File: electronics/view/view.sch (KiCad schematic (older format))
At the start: 90 parts, among them J1 BLDC, J2 USB_C_Receptacle_USB2.0, J3 LCD, J4 Strain, J5 Strain, Q1 MMBT4403, Q2 UMH3N, U1 MT6701-CT, U2 T-Micro32_Plus, U3 CH340C, U4 HX711, U5 TMC6300, U6 AP1117-33, U7 SN74LV1T34DBV, U8 VEML7700

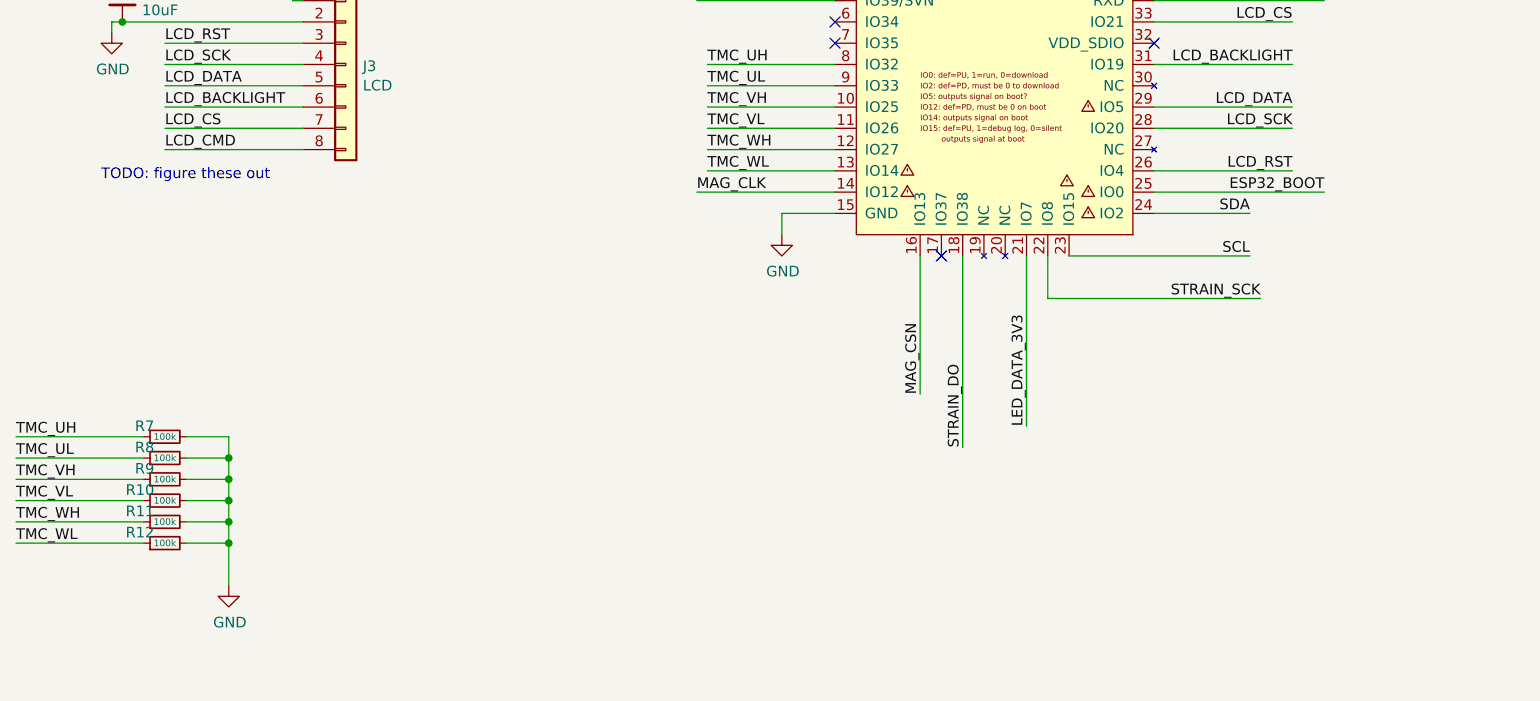
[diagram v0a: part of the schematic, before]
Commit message: View: Update pin assignments on ESP32 to avoid potential boot issues
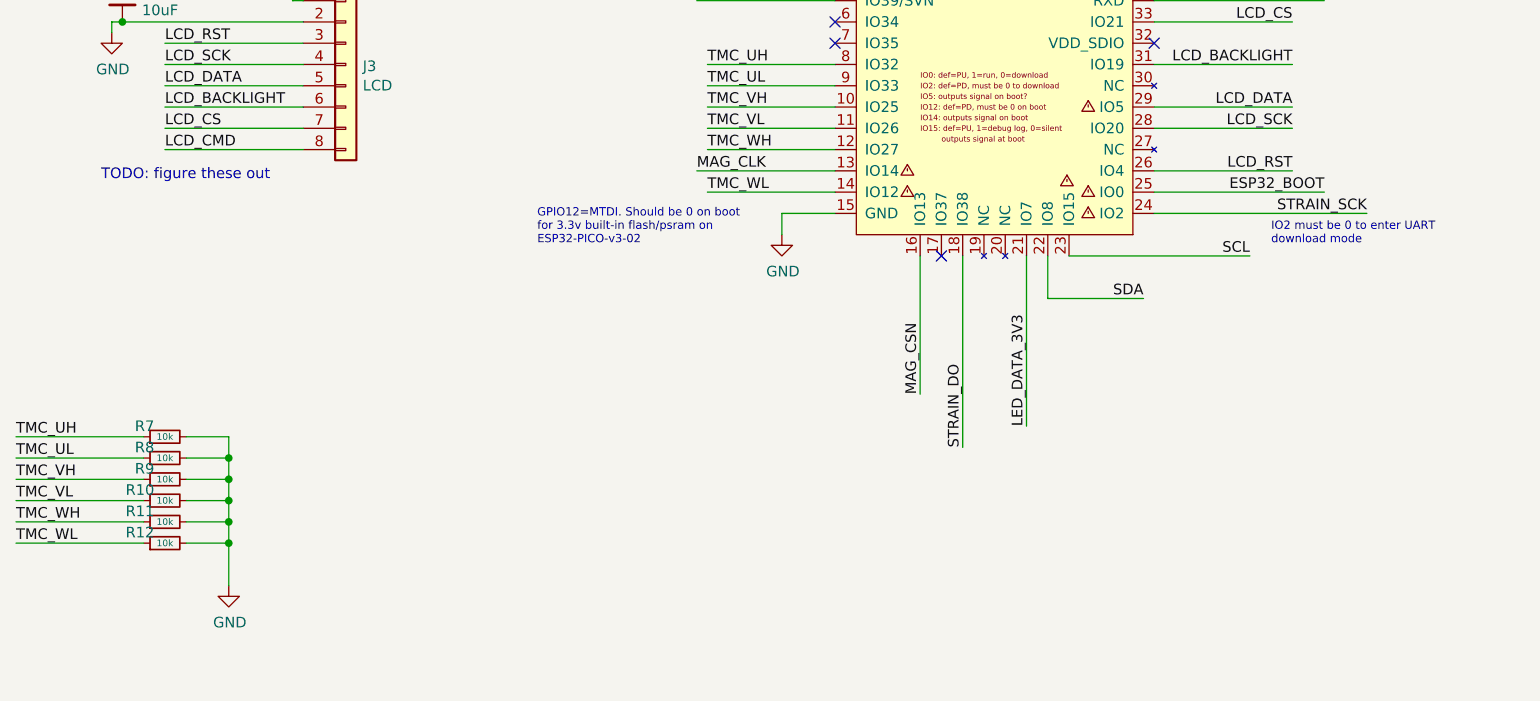
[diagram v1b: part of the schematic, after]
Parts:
- R10, R11, R12, R7, R8, R9: value 100k -> 10k
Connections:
- net MAG_CLK: now also U2.13 (IO14); no longer U2.14 (IO12)
- net SDA: now also U2.22 (IO8); no longer U2.24 (IO2)
- net STRAIN_SCK: now also U2.24 (IO2); no longer U2.22 (IO8)
- net TMC_WL: now also U2.14 (IO12); no longer U2.13 (IO14)
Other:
- note added: "GPIO12=MTDI. Should be 0 on boot\nfor 3.3v built-in flash/psram on\nESP32-PICO-v3-02"
- note added: "IO2 must be 0 to enter UART\ndownload mode"
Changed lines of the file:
@@
 TMC_WH
 Wire Wire Line
-	13050 3450 12450 3450
-Text Label 12450 3450 0    50   ~ 0
+	13050 3550 12450 3550
+Text Label 12450 3550 0    50   ~ 0
 TMC_WL
 Wire Wire Line
@@
 	13450 3850 13450 4500
 Wire Wire Line
-	13050 3550 12400 3550
+	13050 3450 12400 3450
 Wire Wire Line
 	13050 2650 12400 2650
 Text Label 13450 4500 1    50   ~ 0
 MAG_CSN
-Text Label 12400 3550 0    50   ~ 0
+Text Label 12400 3450 0    50   ~ 0
 MAG_CLK
 Text Label 12400 2650 0    50   ~ 0
@@
 Text Label 13650 4750 1    50   ~ 0
 STRAIN_DO
-Text Label 15050 4050 2    50   ~ 0
+Text Label 15550 3650 2    50   ~ 0
 STRAIN_SCK
 Wire Wire Line
-	14050 4050 15050 4050
+	14550 3650 15550 3650
 Wire Wire Line
 	13950 4650 13950 3850
@@
 P 9900 4700
 F 0 "R7" V 9950 4750 50  0000 L CNN
-F 1 "100k" V 9900 4700 31  0000 C CNN
+F 1 "10k" V 9900 4700 31  0000 C CNN
 F 2 "Resistor_SMD:R_0603_1608Metric" H 9900 4700 50  0001 C CNN
 F 3 "~" H 9900 4700 50  0001 C CNN
@@
 P 9900 4800
 F 0 "R8" V 9950 4850 50  0000 L CNN
-F 1 "100k" V 9900 4800 31  0000 C CNN
+F 1 "10k" V 9900 4800 31  0000 C CNN
 F 2 "Resistor_SMD:R_0603_1608Metric" H 9900 4800 50  0001 C CNN
 F 3 "~" H 9900 4800 50  0001 C CNN
@@
 P 9900 4900
 F 0 "R9" V 9950 4950 50  0000 L CNN
-F 1 "100k" V 9900 4900 31  0000 C CNN
+F 1 "10k" V 9900 4900 31  0000 C CNN
 F 2 "Resistor_SMD:R_0603_1608Metric" H 9900 4900 50  0001 C CNN
 F 3 "~" H 9900 4900 50  0001 C CNN
@@
 P 9900 5000
 F 0 "R10" V 9950 5050 50  0000 L CNN
-F 1 "100k" V 9900 5000 31  0000 C CNN
+F 1 "10k" V 9900 5000 31  0000 C CNN
 F 2 "Resistor_SMD:R_0603_1608Metric" H 9900 5000 50  0001 C CNN
 F 3 "~" H 9900 5000 50  0001 C CNN
@@
 P 9900 5100
 F 0 "R11" V 9950 5150 50  0000 L CNN
-F 1 "100k" V 9900 5100 31  0000 C CNN
+F 1 "10k" V 9900 5100 31  0000 C CNN
 F 2 "Resistor_SMD:R_0603_1608Metric" H 9900 5100 50  0001 C CNN
 F 3 "~" H 9900 5100 50  0001 C CNN
@@
 P 9900 5200
 F 0 "R12" V 9950 5250 50  0000 L CNN
-F 1 "100k" V 9900 5200 31  0000 C CNN
+F 1 "10k" V 9900 5200 31  0000 C CNN
 F 2 "Resistor_SMD:R_0603_1608Metric" H 9900 5200 50  0001 C CNN
 F 3 "~" H 9900 5200 50  0001 C CNN
@@
 	14050 4050 14050 3850
 Wire Wire Line
-	14550 3650 15000 3650
+	14050 4050 14500 4050
 Wire Wire Line
 	14150 3850 15000 3850
-Text Label 15000 3650 2    50   ~ 0
+Text Label 14500 4050 2    50   ~ 0
 SDA
 Text Label 15000 3850 2    50   ~ 0
@@
 Wire Wire Line
 	2650 1050 2650 1150
+Text Notes 11650 3800 0    39   ~ 0
+GPIO12=MTDI. Should be 0 on boot\nfor 3.3v built-in flash/psram on\nESP32-PICO-v3-02
+Text Notes 15100 3800 0    39   ~ 0
+IO2 must be 0 to enter UART\ndownload mode
 $EndSCHEMATC

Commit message: View: PCB checkpoint
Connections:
- net MAG_CLK: now also U2.16 (IO13); no longer U2.13 (IO14)
- net MAG_CSN: now also U2.13 (IO14); no longer U2.16 (IO13)
- net MAG_DO: now also U2.17 (IO37); no longer U2.5 (IO39/SVN)
- net SCL: now also U2.22 (IO8); no longer U2.23 (IO15)
- net SDA: now also U2.23 (IO15); no longer U2.22 (IO8)
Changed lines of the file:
@@
 LCD_CMD
 Wire Wire Line
+	13050 3450 12400 3450
+Wire Wire Line
 	13450 3850 13450 4500
 Wire Wire Line
-	13050 3450 12400 3450
-Wire Wire Line
-	13050 2650 12400 2650
+	13550 3850 13550 4500
+Text Label 12400 3450 0    50   ~ 0
+MAG_CSN
 Text Label 13450 4500 1    50   ~ 0
-MAG_CSN
-Text Label 12400 3450 0    50   ~ 0
 MAG_CLK
-Text Label 12400 2650 0    50   ~ 0
+Text Label 13550 4500 1    50   ~ 0
 MAG_DO
 Text Label 13650 4750 1    50   ~ 0
@@
 	14050 4050 14050 3850
 Wire Wire Line
-	14050 4050 14500 4050
-Wire Wire Line
-	14150 3850 15000 3850
-Text Label 14500 4050 2    50   ~ 0
+	14150 3850 14600 3850
+Wire Wire Line
+	14050 4050 14900 4050
+Text Label 14600 3850 2    50   ~ 0
 SDA
-Text Label 15000 3850 2    50   ~ 0
+Text Label 14900 4050 2    50   ~ 0
 SCL
 NoConn ~ 14550 2850
 NoConn ~ 13050 2750
 NoConn ~ 13050 2850
-NoConn ~ 13550 3850
 $Comp
 L power:PWR_FLAG #FLG0101
@@
 Text Notes 15100 3800 0    39   ~ 0
 IO2 must be 0 to enter UART\ndownload mode
+NoConn ~ 13050 2650
 $EndSCHEMATC

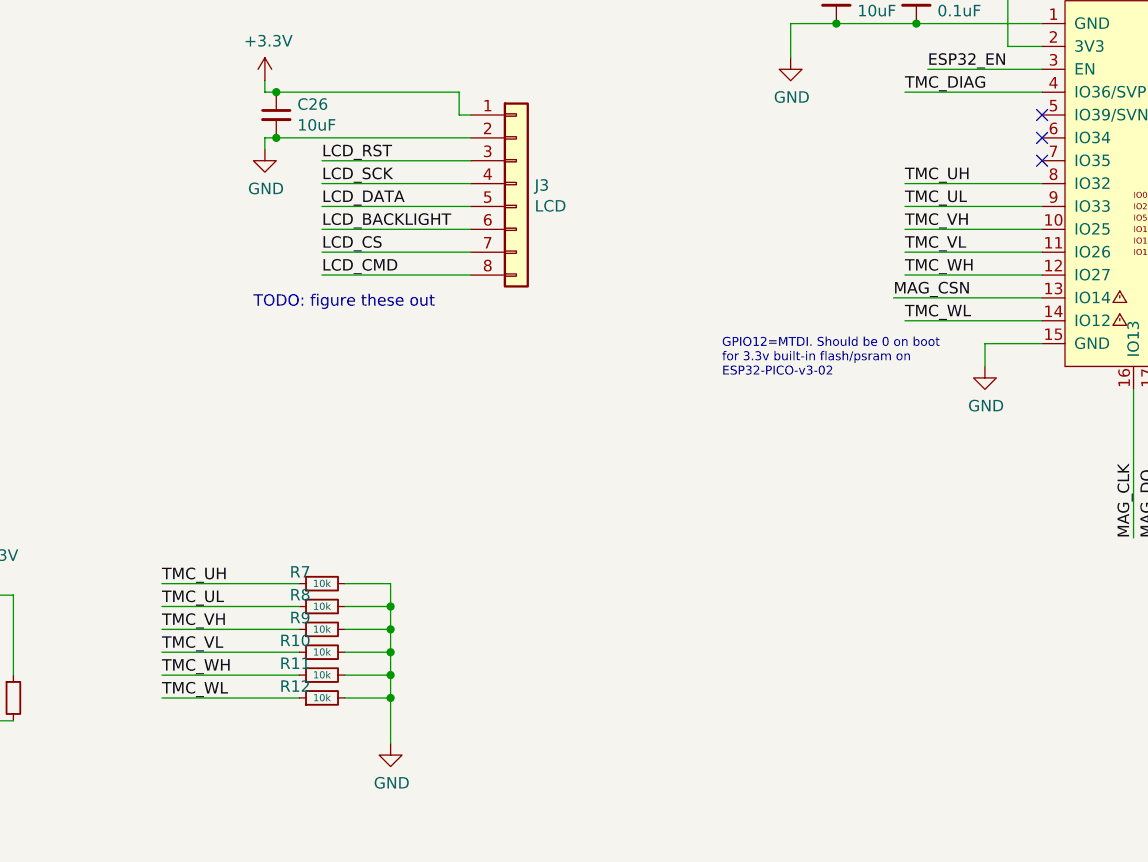
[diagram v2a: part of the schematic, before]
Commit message: View: finished initial routing
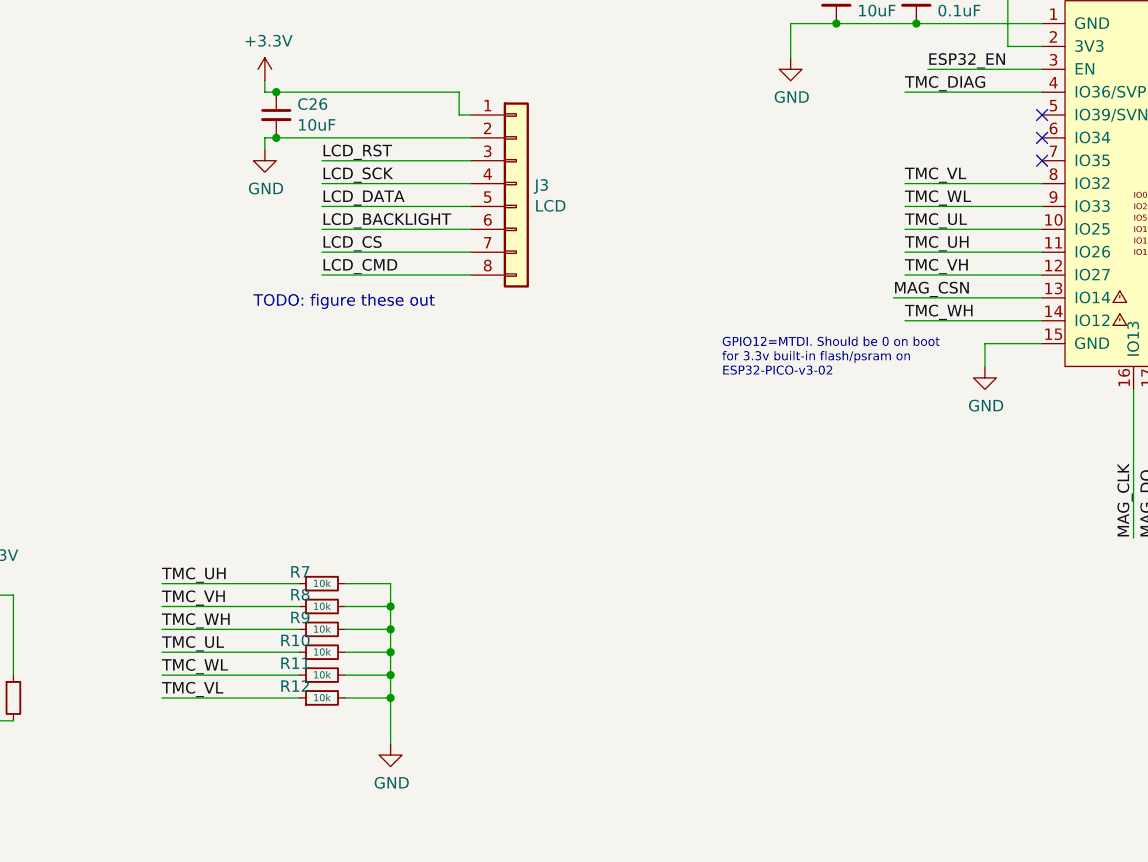
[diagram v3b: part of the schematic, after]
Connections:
- net TMC_UH: now also U2.11 (IO26); no longer U2.8 (IO32)
- net TMC_UL: now also R10.1, U2.10 (IO25); no longer R8.1, U2.9 (IO33)
- net TMC_VH: now also R8.1, U2.12 (IO27); no longer R9.1, U2.10 (IO25)
- net TMC_VL: now also R12.1, U2.8 (IO32); no longer R10.1, U2.11 (IO26)
- net TMC_WH: now also R9.1, U2.14 (IO12); no longer R11.1, U2.12 (IO27)
- net TMC_WL: now also R11.1, U2.9 (IO33); no longer R12.1, U2.14 (IO12)
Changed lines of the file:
@@
 	6700 6500 7050 6500
+Wire Wire Line
+	13050 3150 12450 3150
+Text Label 12450 3150 0    50   ~ 0
+TMC_UL
+Wire Wire Line
+	13050 3350 12450 3350
+Text Label 12450 3350 0    50   ~ 0
+TMC_VH
 Wire Wire Line
 	13050 2950 12450 2950
 Text Label 12450 2950 0    50   ~ 0
-TMC_UH
+TMC_VL
+Wire Wire Line
+	13050 3550 12450 3550
+Text Label 12450 3550 0    50   ~ 0
+TMC_WH
 Wire Wire Line
 	13050 3050 12450 3050
 Text Label 12450 3050 0    50   ~ 0
-TMC_UL
-Wire Wire Line
-	13050 3150 12450 3150
-Text Label 12450 3150 0    50   ~ 0
-TMC_VH
-Wire Wire Line
-	13050 3250 12450 3250
-Text Label 12450 3250 0    50   ~ 0
-TMC_VL
-Wire Wire Line
-	13050 3350 12450 3350
-Text Label 12450 3350 0    50   ~ 0
-TMC_WH
-Wire Wire Line
-	13050 3550 12450 3550
-Text Label 12450 3550 0    50   ~ 0
 TMC_WL
 Wire Wire Line
@@
 TMC_UH
 Wire Wire Line
+	9800 5000 9200 5000
+Text Label 9200 5000 0    50   ~ 0
+TMC_UL
+Wire Wire Line
 	9800 4800 9200 4800
 Text Label 9200 4800 0    50   ~ 0
-TMC_UL
+TMC_VH
+Wire Wire Line
+	9800 5200 9200 5200
+Text Label 9200 5200 0    50   ~ 0
+TMC_VL
 Wire Wire Line
 	9800 4900 9200 4900
 Text Label 9200 4900 0    50   ~ 0
-TMC_VH
-Wire Wire Line
-	9800 5000 9200 5000
-Text Label 9200 5000 0    50   ~ 0
-TMC_VL
+TMC_WH
 Wire Wire Line
 	9800 5100 9200 5100
 Text Label 9200 5100 0    50   ~ 0
-TMC_WH
-Wire Wire Line
-	9800 5200 9200 5200
-Text Label 9200 5200 0    50   ~ 0
 TMC_WL
 $Comp
@@
 IO2 must be 0 to enter UART\ndownload mode
 NoConn ~ 13050 2650
+Text Label 12450 3250 0    50   ~ 0
+TMC_UH
+Wire Wire Line
+	13050 3250 12450 3250
 $EndSCHEMATC

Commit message: Cleanup
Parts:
- added R15, R16: 2.2k, Resistor_SMD:R_0603_1608Metric, symbol Device:R_Small
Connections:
- net +3V3: now also R15.1, R16.2
- net MAG_CLK: now also R16.1
- net MAG_DO: now also R15.2
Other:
- note added: "LCD CONNECTOR"
- note added: "LEDS"
- note added: "MCU - ESP32 (T-MICRO32 PLUS)"
- note added: "MECHANICAL"
- note added: "MOTOR"
- note added: "POWER"
- note added: "PULLUPS, PULLDOWNS"
- note added: "Pull-ups allow for I2C (though\nwe'll primarily use SSI)"
- note added: "SENSOR - AMBIENT LIGHT"
- note added: "SENSOR - MAGNETIC ENCODER"
- note added: "SENSOR - STRAIN"
- note added: "USB"
- moved on the sheet: C12, C13, C14, C15, C16, C17, C18, C19, C20, C21, C22, C23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

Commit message: View: Add initial screen pcb
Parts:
- J3: footprint view_custom:SolderPads_2mm_8 -> SolderPads:SolderPads_2mm_8
- J4, J5: footprint view_custom:SolderPads_2mm_3 -> SolderPads:SolderPads_2mm_3
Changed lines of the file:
@@
 F 0 "J3" H 9980 3192 50  0000 L CNN
 F 1 "LCD" H 9980 3101 50  0000 L CNN
-F 2 "view_custom:SolderPads_2mm_8" H 9900 3200 50  0001 C CNN
+F 2 "SolderPads:SolderPads_2mm_8" H 9900 3200 50  0001 C CNN
 F 3 "~" H 9900 3200 50  0001 C CNN
 	1    9900 3200
@@
 F 0 "J4" H 5530 7492 50  0000 L CNN
 F 1 "Strain" H 5530 7401 50  0000 L CNN
-F 2 "view_custom:SolderPads_2mm_3" H 5450 7450 50  0001 C CNN
+F 2 "SolderPads:SolderPads_2mm_3" H 5450 7450 50  0001 C CNN
 F 3 "~" H 5450 7450 50  0001 C CNN
 	1    5450 7450
@@
 F 0 "J5" H 5530 7942 50  0000 L CNN
 F 1 "Strain" H 5530 7851 50  0000 L CNN
-F 2 "view_custom:SolderPads_2mm_3" H 5450 7900 50  0001 C CNN
+F 2 "SolderPads:SolderPads_2mm_3" H 5450 7900 50  0001 C CNN
 F 3 "~" H 5450 7900 50  0001 C CNN
 	1    5450 7900
